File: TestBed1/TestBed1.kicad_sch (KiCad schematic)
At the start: 1 part, among them J2 Conn_01x04_Pin

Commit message: WIP Adding new sheets.
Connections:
- net VCC renamed CAN_VCC
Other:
- added sheet CANBus (CANBus.kicad_sch)
- added sheet LEDs (LEDs.kicad_sch)
- added sheet Power (Power.kicad_sch)
- sheet MCU ports: added CANComs; removed CANH, CANL
- note removed: "TODO LEDs?"
- note removed: "TODO Power"
- note removed: "TODO Power filter?"
- note removed: "TODO what comes from controller? 12V? or 5V? design to accept up to 24v?"
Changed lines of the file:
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@@
 	(bus
 		(pts
-			(xy 76.2 132.08) (xy 85.09 132.08)
+			(xy 67.31 121.92) (xy 67.31 113.03)
+		)
+		(stroke
+			(width 0)
+			(type default)
+		)
+	)
+	(bus
+		(pts
+			(xy 76.2 132.08) (xy 92.71 132.08)
 		)
 		(stroke
@@
 	(bus
 		(pts
+			(xy 67.31 113.03) (xy 71.12 113.03)
+		)
+		(stroke
+			(width 0)
+			(type default)
+		)
+	)
+	(bus
+		(pts
 			(xy 74.93 157.48) (xy 74.93 144.78)
 		)
@@
 	(bus
 		(pts
+			(xy 71.12 113.03) (xy 71.12 104.14)
+		)
+		(stroke
+			(width 0)
+			(type default)
+		)
+	)
+	(bus
+		(pts
 			(xy 64.77 157.48) (xy 64.77 144.78)
 		)
@@
 		)
 	)
-	(text "TODO what comes from controller? 12V? or 5V? design to accept up to 24v?"
-		(exclude_from_sim no)
-		(at 112.268 55.118 0)
-		(effects
-			(font
-				(size 1.27 1.27)
-			)
-		)
-	)
-	(text "TODO LEDs?"
-		(exclude_from_sim no)
-		(at 83.82 128.27 0)
-		(effects
-			(font
-				(size 1.27 1.27)
-			)
-		)
-	)
-	(text "TODO Power"
-		(exclude_from_sim no)
-		(at 135.128 58.166 0)
-		(effects
-			(font
-				(size 1.27 1.27)
-			)
-		)
-	)
-	(text "TODO Power filter?"
-		(exclude_from_sim no)
-		(at 134.874 60.96 0)
-		(effects
-			(font
-				(size 1.27 1.27)
-			)
+	(label "CAN_VCC"
+		(at 107.95 83.82 90)
+		(effects
+			(font
+				(size 1.27 1.27)
+			)
+			(justify left bottom)
 		)
 	)
 	(label "CANH"
-		(at 57.15 121.92 90)
-		(fields_autoplaced yes)
+		(at 76.2 86.36 0)
 		(effects
 			(font
@@
 	(label "CANH"
 		(at 152.4 60.96 180)
-		(fields_autoplaced yes)
 		(effects
 			(font
@@
 			)
 			(justify right bottom)
-		)
-	)
-	(label "CANL"
-		(at 59.69 121.92 90)
-		(fields_autoplaced yes)
-		(effects
-			(font
-				(size 1.27 1.27)
-			)
-			(justify left bottom)
 		)
 	)
 	(label "GND"
 		(at 152.4 66.04 180)
-		(fields_autoplaced yes)
 		(effects
 			(font
@@
 		)
 	)
-	(label "VCC"
+	(label "CAN_VCC"
 		(at 152.4 58.42 180)
-		(fields_autoplaced yes)
 		(effects
 			(font
@@
 			)
 			(justify right bottom)
+		)
+	)
+	(label "CANL"
+		(at 76.2 88.9 0)
+		(effects
+			(font
+				(size 1.27 1.27)
+			)
+			(justify left bottom)
 		)
 	)
 	(label "CANL"
 		(at 152.4 63.5 180)
-		(fields_autoplaced yes)
 		(effects
 			(font
@@
 			)
 		)
-		(pin "CANH" input
-			(at 57.15 121.92 90)
-			(effects
-				(font
-					(size 1.27 1.27)
-				)
-				(justify right)
-			)
-		)
-		(pin "CANL" input
-			(at 59.69 121.92 90)
+		(pin "CANComs" input
+			(at 67.31 121.92 90)
 			(effects
 				(font
@@
 	)
 	(sheet
+		(at 46.99 83.82)
+		(size 29.21 20.32)
+		(fields_autoplaced yes)
+		(stroke
+			(width 0.1524)
+			(type solid)
+		)
+		(fill
+			(color 0 0 0 0.0000)
+		)
+		(property "Sheetname" "CANBus"
+			(at 46.99 83.1084 0)
+			(effects
+				(font
+					(size 1.27 1.27)
+				)
+				(justify left bottom)
+			)
+		)
+		(property "Sheetfile" "CANBus.kicad_sch"
+			(at 46.99 104.7246 0)
+			(effects
+				(font
+					(size 1.27 1.27)
+				)
+				(justify left top)
+			)
+		)
+		(pin "CANComs" input
+			(at 71.12 104.14 270)
+			(effects
+				(font
+					(size 1.27 1.27)
+				)
+				(justify left)
+			)
+		)
+		(pin "CANH" input
+			(at 76.2 86.36 0)
+			(effects
+				(font
+					(size 1.27 1.27)
+				)
+				(justify right)
+			)
+		)
+		(pin "CANL" input
+			(at 76.2 88.9 0)
+			(effects
+				(font
+					(size 1.27 1.27)
+				)
+				(justify right)
+			)
+		)
+		(instances
+			(project "TestBed1"
+				(path "/1011cb81-baf2-4a82-93dd-e89e67a76dd8"
+					(page "5")
+				)
+			)
+		)
+	)
+	(sheet
 		(at 49.53 157.48)
 		(size 27.94 22.86)
@@
 				)
 			)
+		)
+	)
+	(sheet
+		(at 95.25 83.82)
+		(size 22.86 20.32)
+		(fields_autoplaced yes)
+		(stroke
+			(width 0.1524)
+			(type solid)
+		)
+		(fill
+			(color 0 0 0 0.0000)
+		)
+		(property "Sheetname" "Power"
+			(at 95.25 83.1084 0)
+			(effects
+				(font
+					(size 1.27 1.27)
+				)
+				(justify left bottom)
+			)
+		)
+		(property "Sheetfile" "Power.kicad_sch"
+			(at 95.25 104.7246 0)
+			(effects
+				(font
+					(size 1.27 1.27)
+				)
+				(justify left top)
+			)
+		)
+		(pin "CAN_VCC" input
+			(at 107.95 83.82 90)
+			(effects
+				(font
+					(size 1.27 1.27)
+				)
+				(justify right)
+			)
+		)
+		(instances
+			(project "TestBed1"
+				(path "/1011cb81-baf2-4a82-93dd-e89e67a76dd8"
+					(page "6")
+				)
+			)
+		)
+	)
+	(sheet
+		(at 92.71 121.92)
+		(size 20.32 20.32)
+		(fields_autoplaced yes)
+		(stroke
+			(width 0.1524)
+			(type solid)
+		)
+		(fill
+			(color 0 0 0 0.0000)
+		)
+		(property "Sheetname" "LEDs"
+			(at 92.71 121.2084 0)
+			(effects
+				(font
+					(size 1.27 1.27)
+				)
+				(justify left bottom)
+			)
+		)
+		(property "Sheetfile" "LEDs.kicad_sch"
+			(at 92.71 142.8246 0)
+			(effects
+				(font
+					(size 1.27 1.27)
+				)
+				(justify left top)
+			)
+		)
+		(pin "LEDs" input
+			(at 92.71 132.08 180)
+			(effects
+				(font
+					(size 1.27 1.27)
+				)
+				(justify left)
+			)
+		)
+		(instances
+			(project "TestBed1"
+				(path "/1011cb81-baf2-4a82-93dd-e89e67a76dd8"
+					(page "4")
+				)
+			)

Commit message: WIP - Parts Assigned
Need footprints, and MCU connections, but WIP
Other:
- note added: "TODO Buzzer?"
- note added: "TODO any filtering on CAN VCC?"
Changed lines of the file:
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@@
+		)
+	)
+	(text "TODO any filtering on CAN VCC?"
+		(exclude_from_sim no)
+		(at 119.888 57.404 0)
+		(effects
+			(font
+				(size 1.27 1.27)
+			)
+		)
+	)
+	(text "TODO Buzzer?"
+		(exclude_from_sim no)
+		(at 157.988 122.174 0)
+		(effects
+			(font
+				(size 1.27 1.27)
+			)
 		)
 	)
@@
 		)
 		(pin "CAN_VCC" input
-			(at 107.95 83.82 90)
-			(effects
-				(font
+			(at 105.41 83.82 90)
+			(effects
+				(font

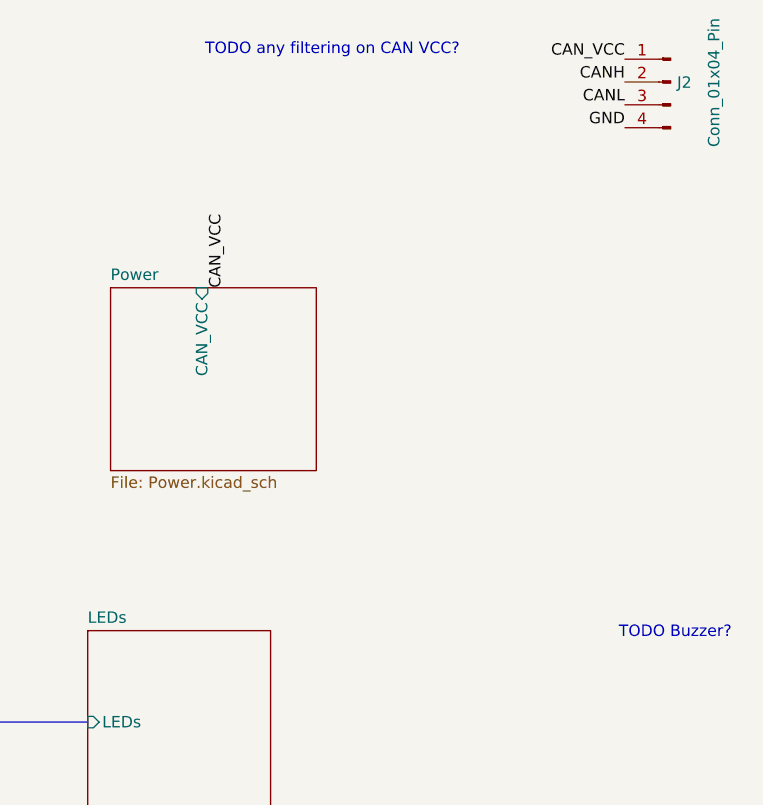
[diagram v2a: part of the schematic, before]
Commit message: Rough Grouping, Passive Footprint Assignment
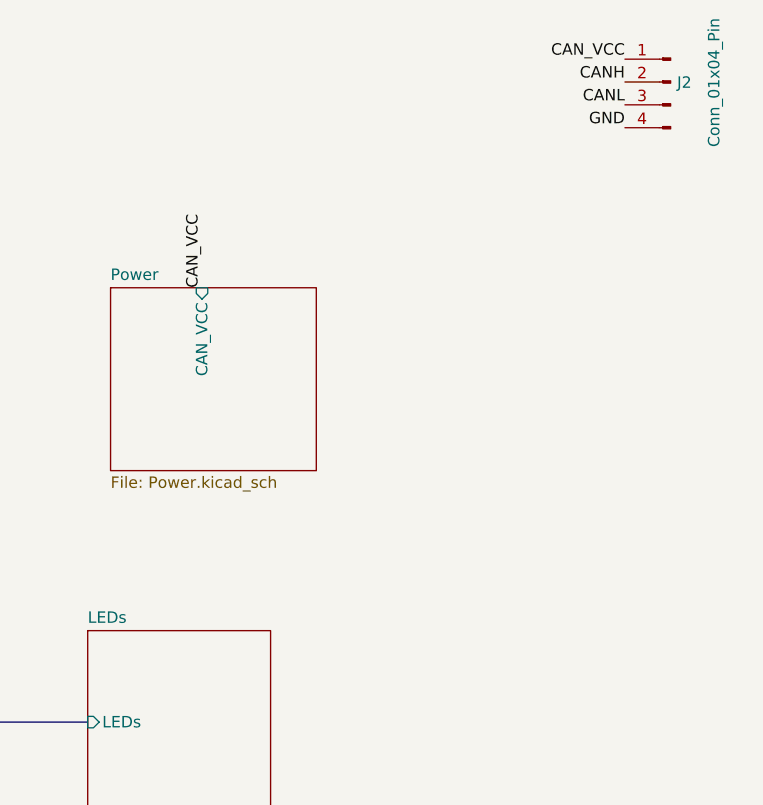
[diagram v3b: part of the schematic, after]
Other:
- note removed: "TODO Buzzer?"
- note removed: "TODO any filtering on CAN VCC?"
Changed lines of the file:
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@@
-		)
-	)
-	(text "TODO any filtering on CAN VCC?"
-		(exclude_from_sim no)
-		(at 119.888 57.404 0)
-		(effects
-			(font
-				(size 1.27 1.27)
-			)
-		)
-	)
-	(text "TODO Buzzer?"
-		(exclude_from_sim no)
-		(at 157.988 122.174 0)
-		(effects
-			(font
-				(size 1.27 1.27)
-			)
 		)
 	)
 	(label "CAN_VCC"
-		(at 107.95 83.82 90)
+		(at 105.41 83.82 90)
 		(effects
 			(font

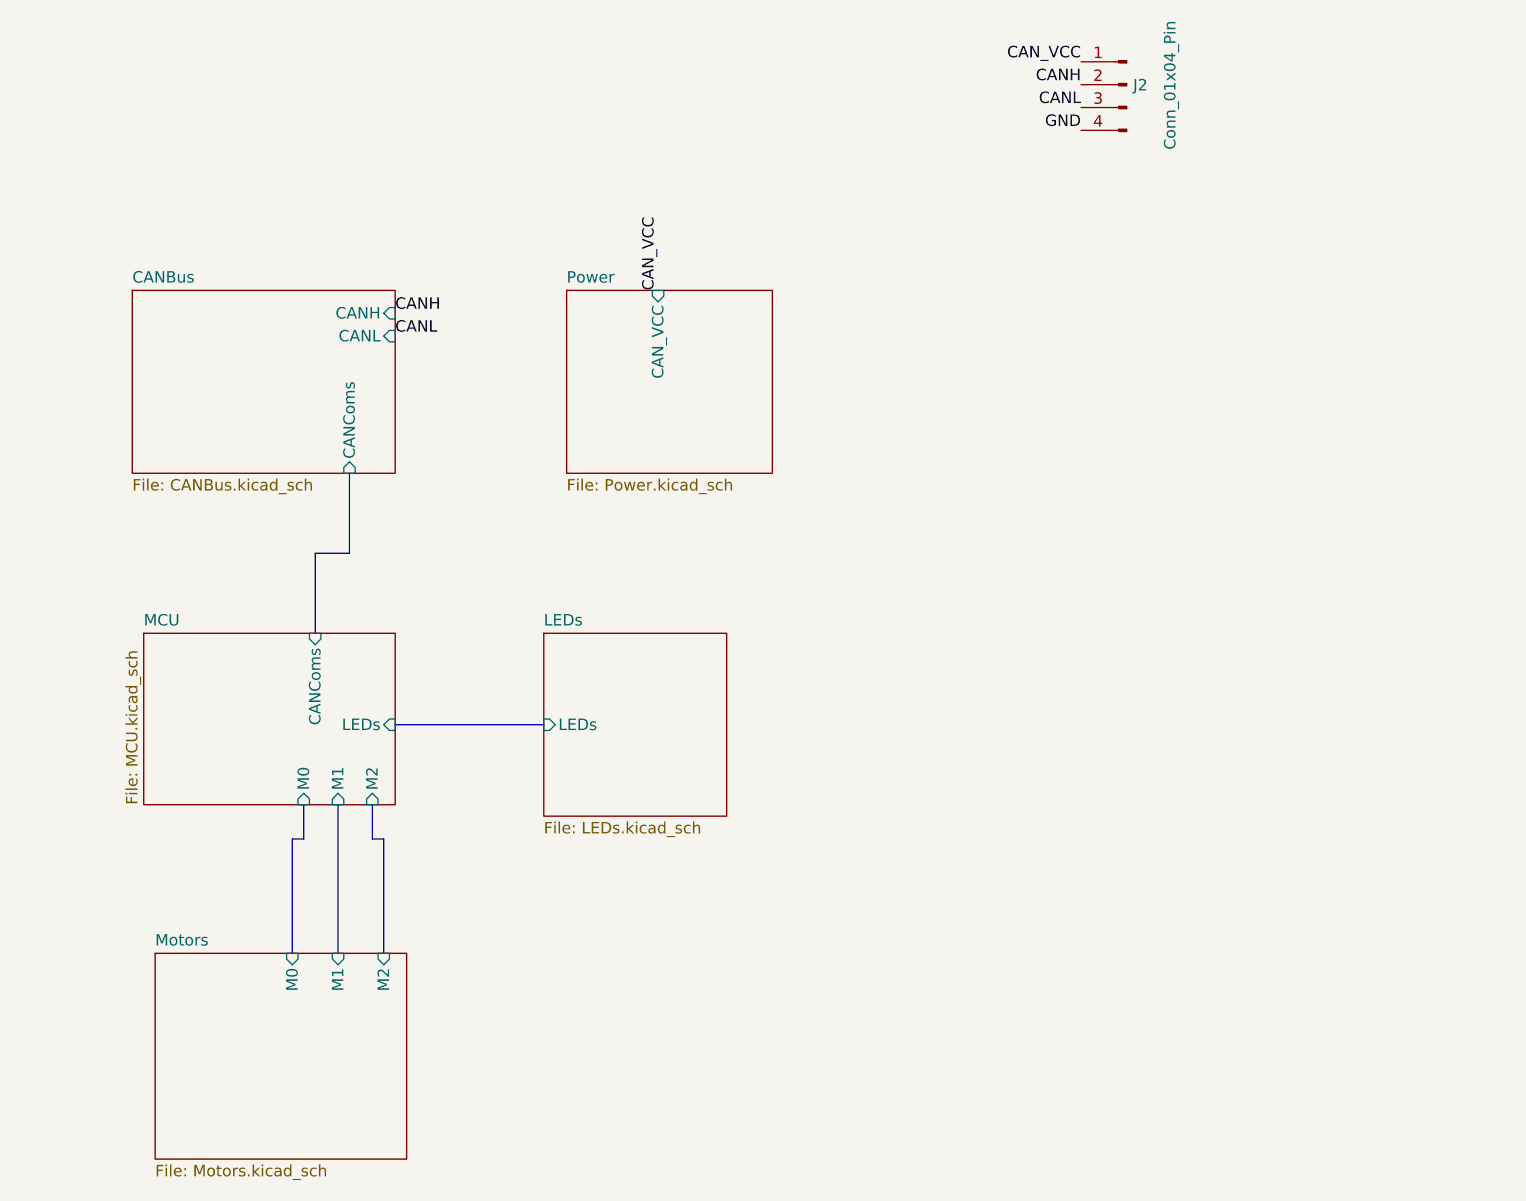
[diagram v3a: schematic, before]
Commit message: Schematic Assignment, board assignemtn and rough placement
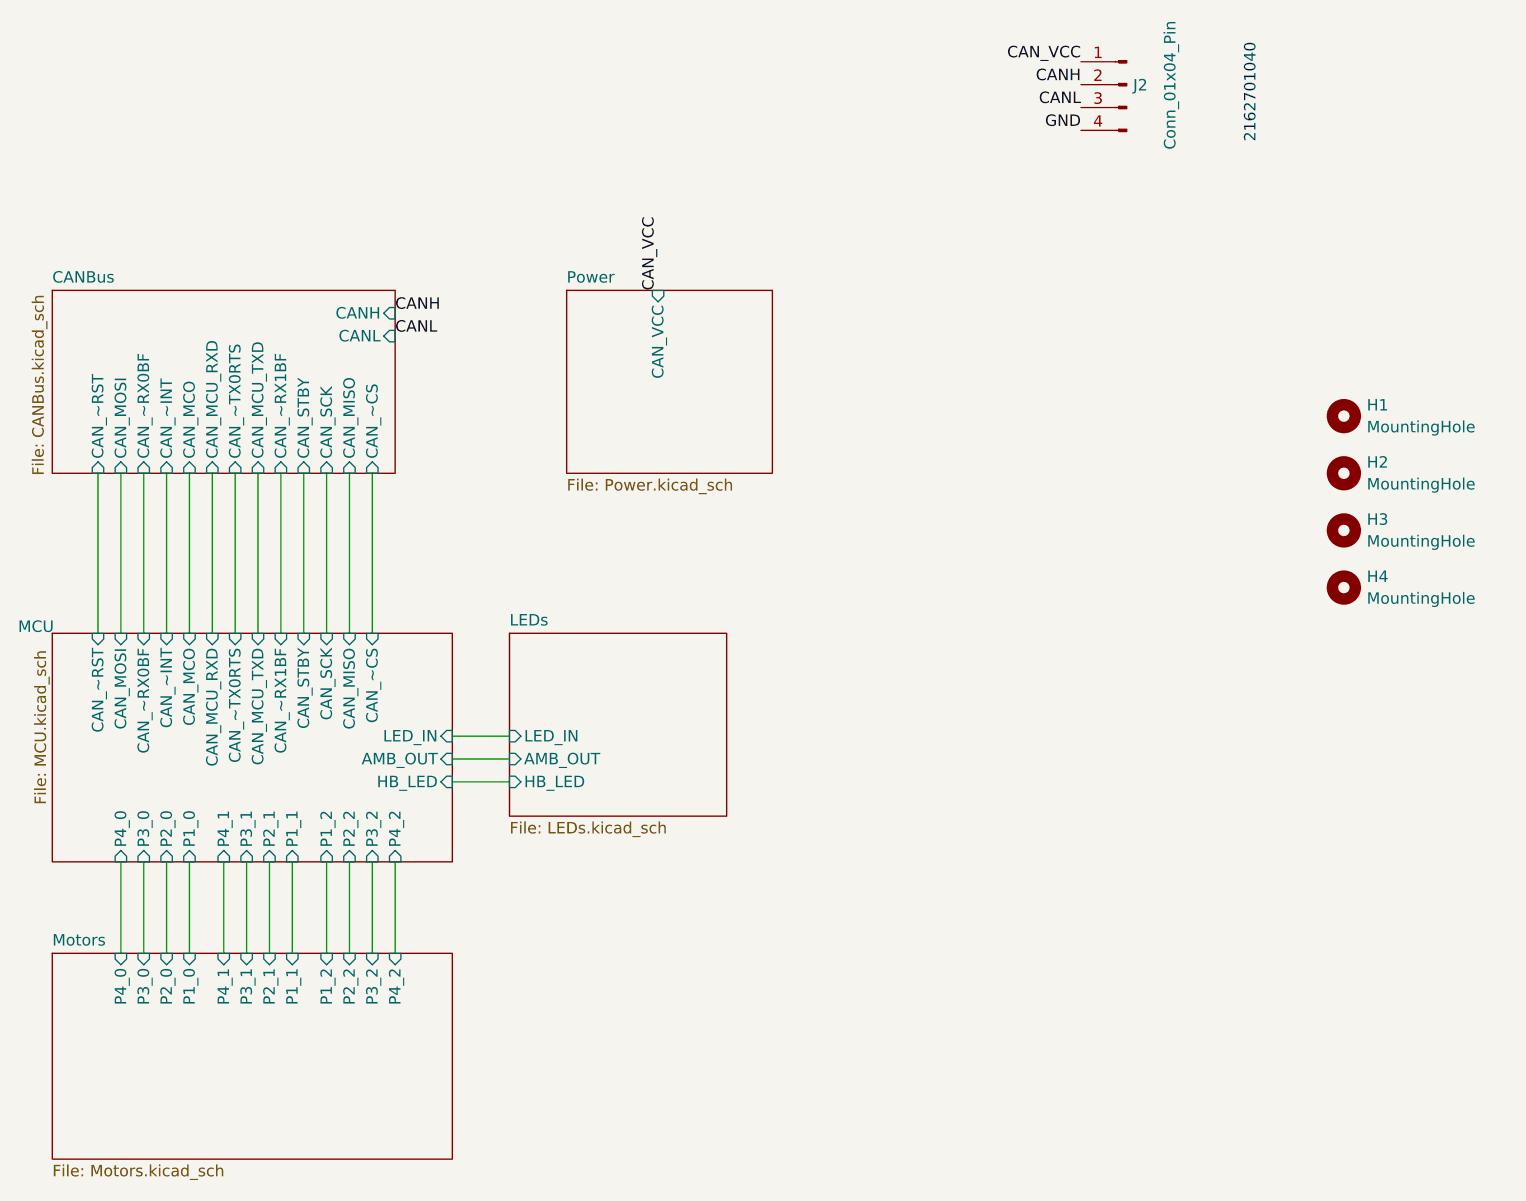
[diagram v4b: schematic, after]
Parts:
- added H1, H2, H3, H4: MountingHole, MountingHole:MountingHole_3.2mm_M3, symbol Mechanical:MountingHole
- J2: footprint (none) -> X27:CONN_70551-xxxx_04_MOL
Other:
- sheet CANBus ports: added CAN_MCO, CAN_MCU_RXD, CAN_MCU_TXD, CAN_MISO, CAN_MOSI, CAN_SCK, CAN_STBY, CAN_~CS, CAN_~INT, CAN_~RST, CAN_~RX0BF, CAN_~RX1BF, CAN_~TX0RTS; removed CANComs
- sheet LEDs ports: added AMB_OUT, HB_LED, LED_IN; removed LEDs
- sheet MCU ports: added AMB_OUT, CAN_MCO, CAN_MCU_RXD, CAN_MCU_TXD, CAN_MISO, CAN_MOSI, CAN_SCK, CAN_STBY, CAN_~CS, CAN_~INT, CAN_~RST, CAN_~RX0BF, CAN_~RX1BF, CAN_~TX0RTS, HB_LED, LED_IN, P1_0, P1_1, P1_2, P2_0, P2_1, P2_2, P3_0, P3_1, P3_2, P4_0, P4_1, P4_2; removed CANComs, LEDs, M0, M1, M2
- sheet Motors ports: added P1_0, P1_1, P1_2, P2_0, P2_1, P2_2, P3_0, P3_1, P3_2, P4_0, P4_1, P4_2; removed M0, M1, M2
- note added: "2162701040"

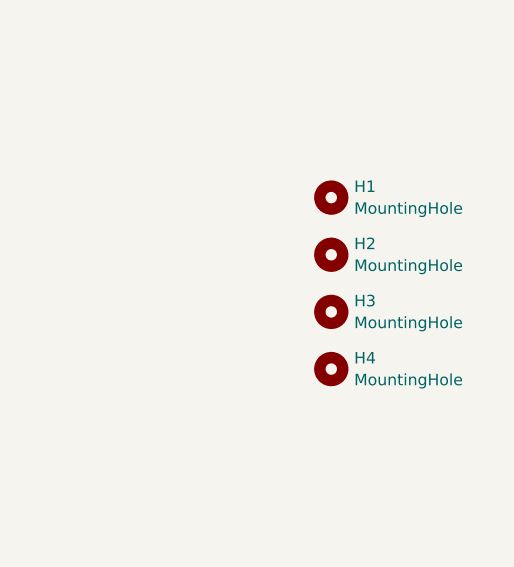
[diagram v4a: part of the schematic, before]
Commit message: Rough Placement and board outline
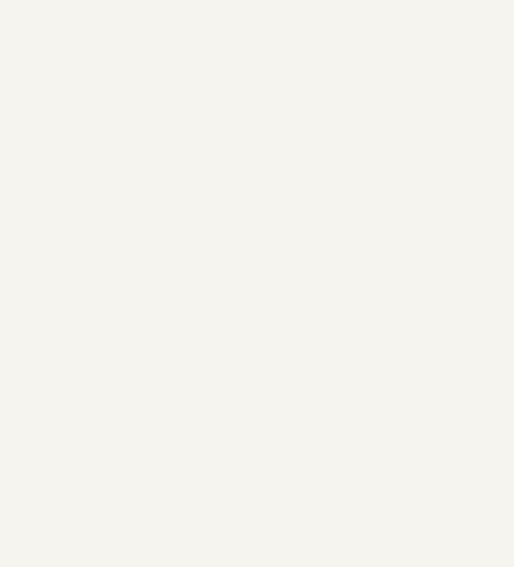
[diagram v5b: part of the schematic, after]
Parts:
- removed H1, H2, H3, H4: MountingHole, MountingHole:MountingHole_3.2mm_M3, symbol Mechanical:MountingHole
